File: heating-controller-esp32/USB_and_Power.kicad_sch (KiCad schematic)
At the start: 9 parts

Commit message: Initial design of schematic complete. Started laying out PCB
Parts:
- removed C40, C41: ~, symbol Device:C
- removed C42: ~, symbol ecu-controller-rescue:CP-Device
- removed J3: ~, symbol Connector:USB_C_Receptacle_USB2.0
- added C11, C8: 10nF/100V, Capacitor_SMD:C_0603_1608Metric, symbol Device:C
- added C12: 10uF, Capacitor_SMD:C_1206_3216Metric, symbol ecu-controller-rescue:CP-Device
- added J11: USB_C_Receptacle_USB2.0, Connector_USB:USB_C_Receptacle_HRO_TYPE-C-31-M-12, symbol Connector:USB_C_Receptacle_USB2.0
- FB1: value ~ -> Ferrite_Bead; footprint (none) -> Inductor_SMD:L_0805_2012Metric
- R23: value ~ -> 1M
- R24: value ~ -> 5.1K
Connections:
- net GND: now also C11.2, C12.2, C8.2, J11.A1 (GND), J11.A12 (GND), J11.B1 (GND), J11.B12 (GND)
- net USB_D+: now also J11.A6 (D+), J11.B6 (D+)
- net USB_D-: now also J11.A7 (D-), J11.B7 (D-)
- net VBUS: now also C11.1, C12.1
- net at R25.1: now also J11.A5 (CC1)
- net at FB1.2, U5.5 (VBUS): now also C8.1, J11.A4 (VBUS), J11.A9 (VBUS), J11.B4 (VBUS), J11.B9 (VBUS)
- net at R24.1: now also J11.B5 (CC2)
- net at R23.2: now also J11.S1 (SHIELD)

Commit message: Mounting holes, a few more tweaks
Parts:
- R24: LCSC (none) -> C23186
- R25: value ~ -> 4.7K; LCSC (none) -> C23162
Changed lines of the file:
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@@
       (effects (font (size 1.778 1.778)) (justify bottom))
     )
-    (property "Value" "~" (id 1) (at 132.08 85.344 90)
+    (property "Value" "4.7K" (id 1) (at 132.08 85.344 90)
       (effects (font (size 1.778 1.778)) (justify top))
     )
@@
     )
     (property "Datasheet" "~" (id 3) (at 132.08 83.82 0)
+      (effects (font (size 1.27 1.27)) hide)
+    )
+    (property "LCSC" "C23162" (id 4) (at 132.08 83.82 0)
       (effects (font (size 1.27 1.27)) hide)
     )
@@
       (effects (font (size 1.27 1.27)) hide)
     )
+    (property "LCSC" "C23186" (id 4) (at 124.46 83.82 0)
+      (effects (font (size 1.27 1.27)) hide)
+    )

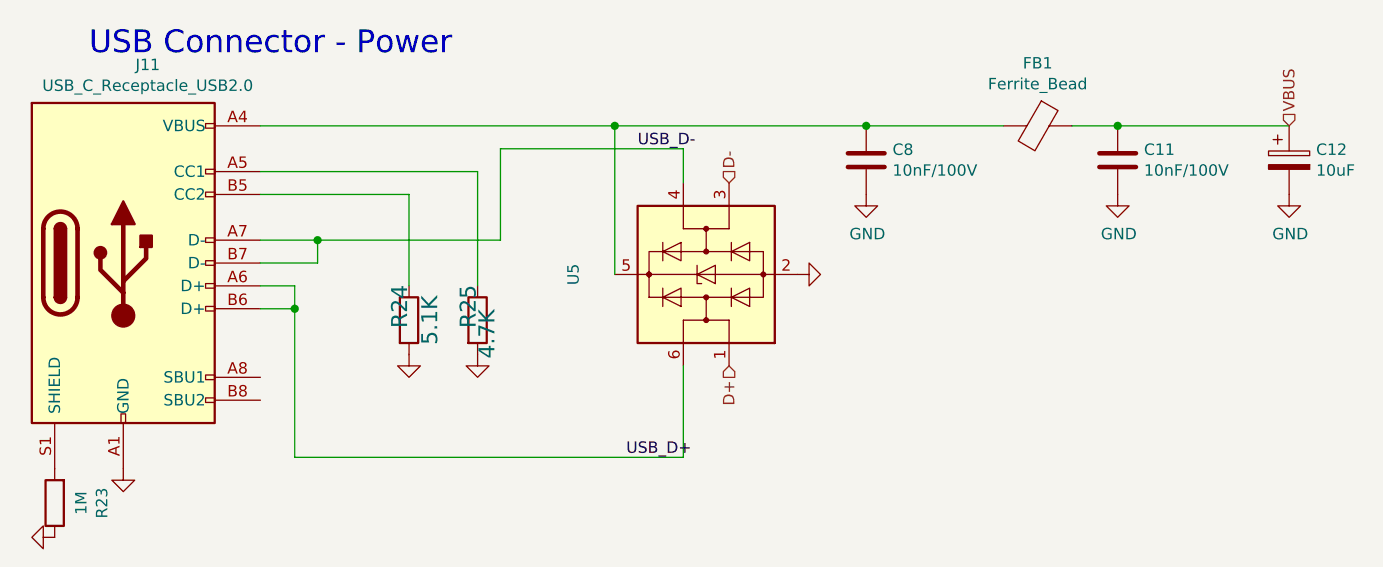
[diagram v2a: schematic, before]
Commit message: Oops. Missing certain files for commit.
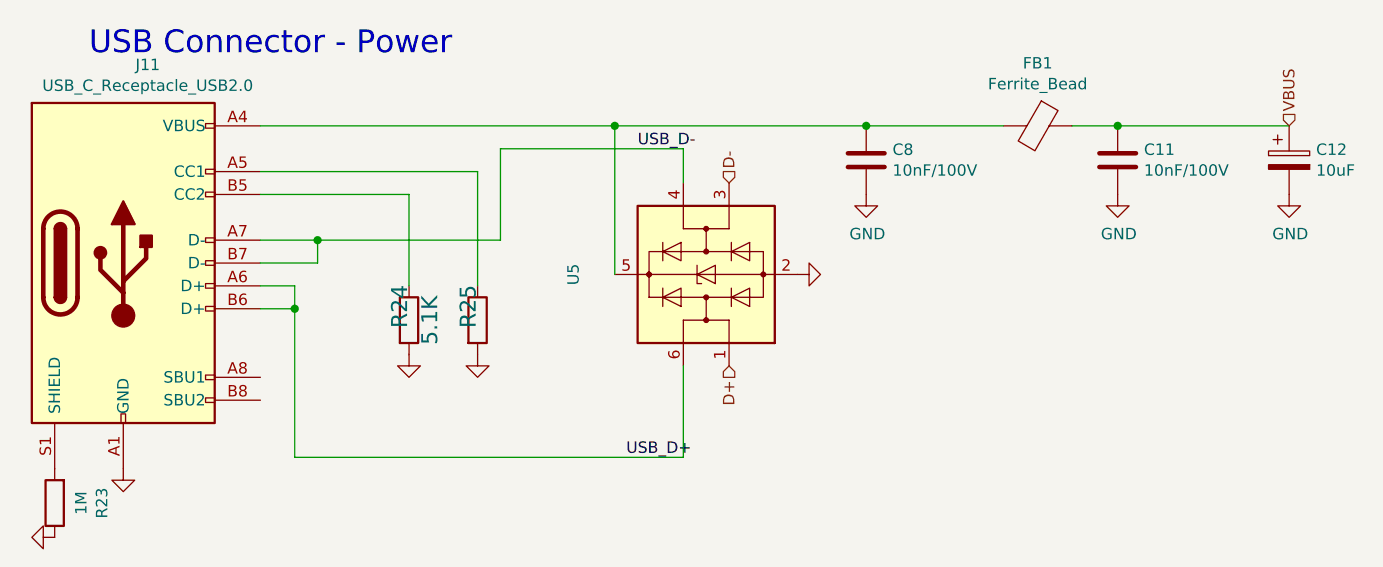
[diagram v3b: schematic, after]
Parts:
- R25: value 4.7K -> ~
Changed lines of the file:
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@@
       (effects (font (size 1.778 1.778)) (justify bottom))
     )
-    (property "Value" "4.7K" (id 1) (at 132.08 85.344 90)
+    (property "Value" "~" (id 1) (at 132.08 85.344 90)
       (effects (font (size 1.778 1.778)) (justify top))
     )

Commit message: Changes for JLCB fabrication using https://github.com/Bouni/kicad-jlcpcb-tools
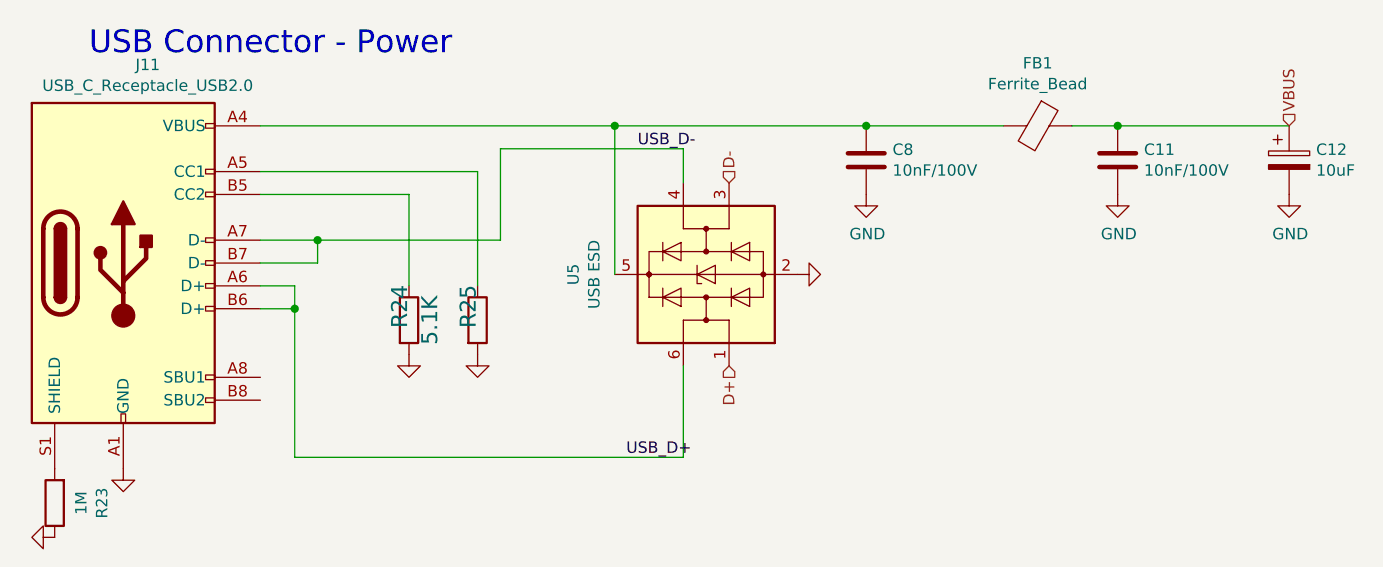
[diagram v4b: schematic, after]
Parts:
- R25: value ~ -> 5.1K
- U5: value ~ -> USB ESD
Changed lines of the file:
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@@
       (effects (font (size 1.778 1.778)) (justify bottom))
     )
-    (property "Value" "~" (id 1) (at 132.08 85.344 90)
-      (effects (font (size 1.778 1.778)) (justify top))
+    (property "Value" "5.1K" (id 1) (at 132.08 85.344 90)
+      (effects (font (size 1.778 1.778)) (justify top) hide)
     )
     (property "Footprint" "Resistor_SMD:R_0603_1608Metric" (id 2) (at 132.08 83.82 0)
@@
     (in_bom yes) (on_board yes)
     (property "Reference" "U5" (id 0) (at 142.7226 78.74 0))
-    (property "Value" "~" (id 1) (at 145.034 78.74 0))
+    (property "Value" "USB ESD" (id 1) (at 145.034 78.74 0))
     (property "Footprint" "Package_TO_SOT_SMD:SOT-666" (id 2) (at 170.18 78.74 0)
       (effects (font (size 1.27 1.27)) hide)
